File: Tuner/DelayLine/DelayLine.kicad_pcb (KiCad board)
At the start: 2 copper layers, 100 x 100 mm, 84 parts, among them J1 Conn_Coaxial, J10 Conn_Coaxial, J11 Conn_Coaxial, J12 Conn_Coaxial, J13 Conn_01x01, J14 Conn_01x01, J15 Conn_01x01, J16 Conn_01x01, J17 Conn_02x10_Odd_Even, J18 Conn_Coaxial, J19 Conn_Coaxial, J2 Conn_Coaxial, J20 Conn_Coaxial, J21 Conn_Coaxial, J22 Conn_Coaxial, J23 Conn_Coaxial, J24 Conn_Coaxial, J25 Conn_01x01, J26 Conn_01x01, J27 Conn_01x01, J28 Conn_01x01, J29 Conn_Coaxial, J3 Conn_Coaxial, J30 Conn_Coaxial, J31 Conn_Coaxial, J4 Conn_Coaxial, J5 Conn_Coaxial, J6 Conn_Coaxial, J7 Conn_Coaxial, J8 Conn_01x02, J9 Conn_01x02

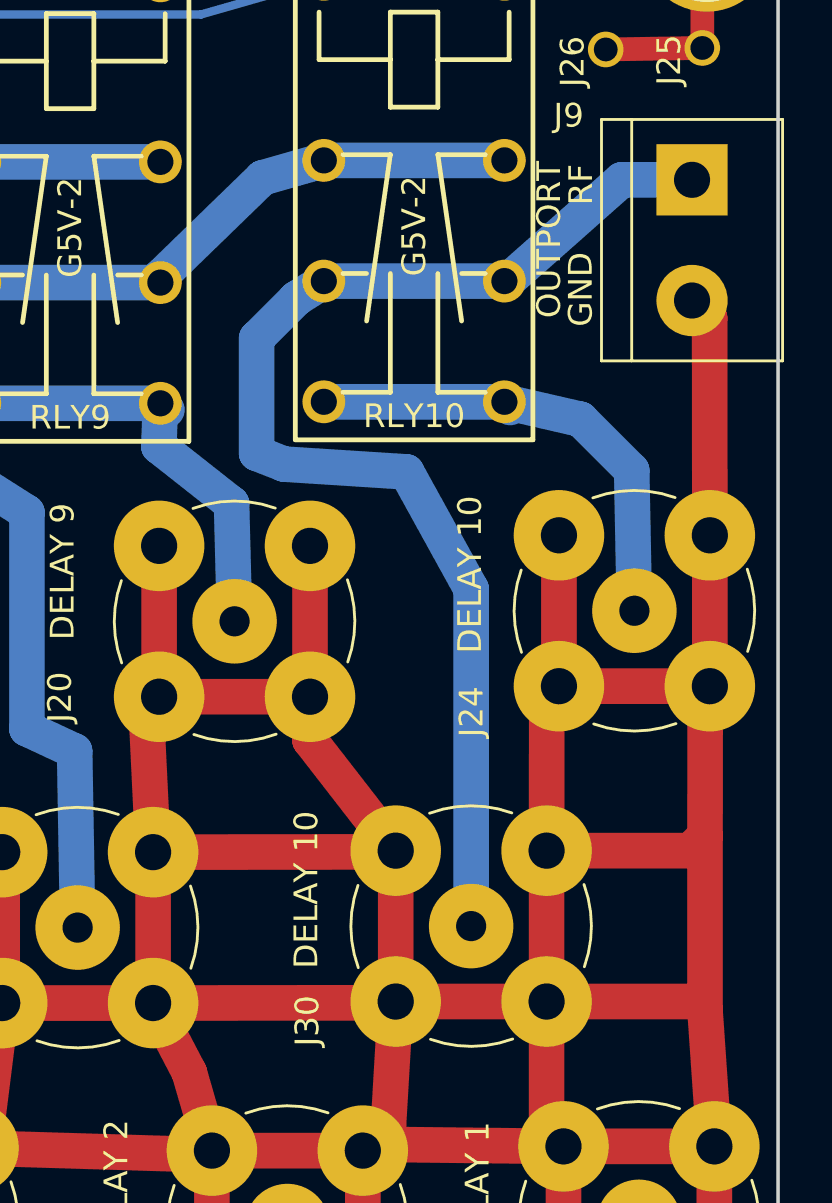
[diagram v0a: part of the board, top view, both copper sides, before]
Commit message: Added phase reversal transformer
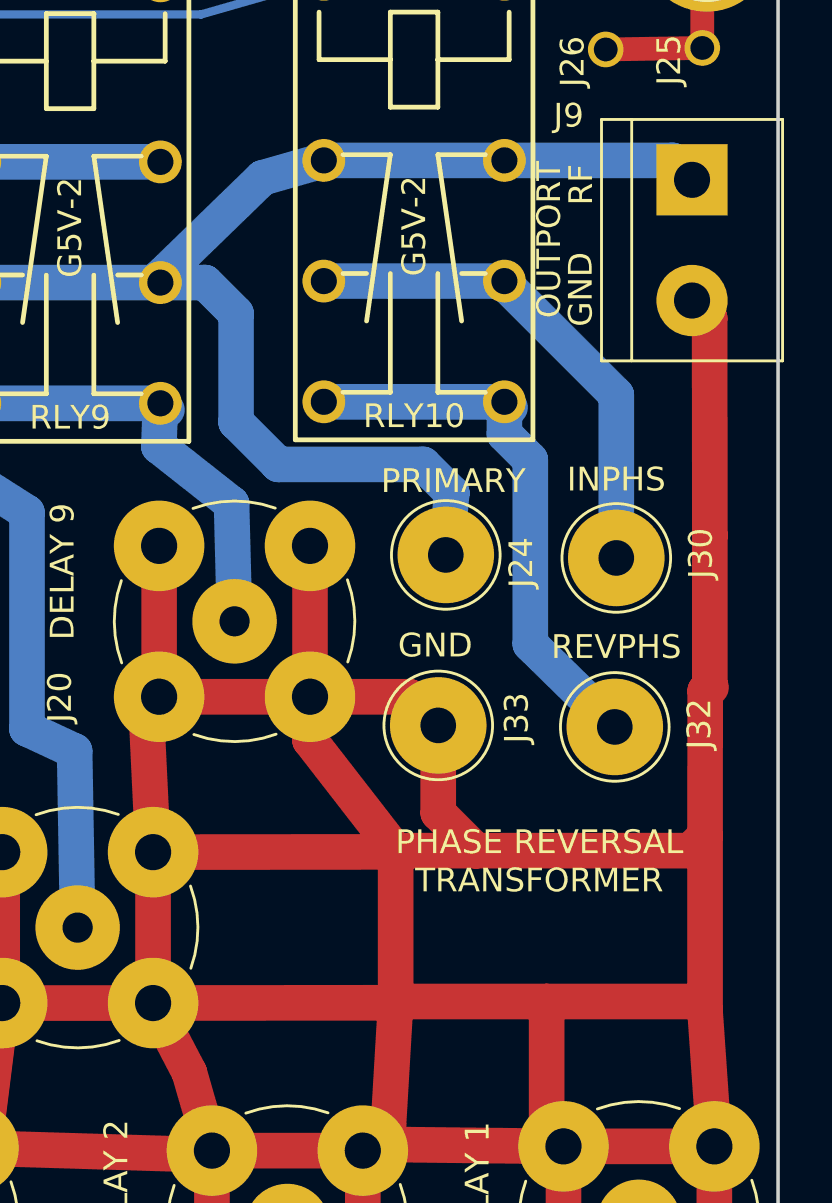
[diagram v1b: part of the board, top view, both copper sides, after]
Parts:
- added J32: Conn_01x01, Connectors:1pin, F.Cu at (143.1, 85.9)
- added J33: Conn_01x01, Connectors:1pin, F.Cu at (135.7, 85.8)
- J24, J30: value Conn_Coaxial -> Conn_01x01; footprint Connectors:bnc-ci -> Connectors:1pin
- moved J30 16.7 mm to (143.2, 78.7)
- moved J24 8.28 mm to (136.0, 78.6)
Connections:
- J24 pad 1: Net-(J24-Pad1) -> Net-(J22-Pad1)
- J9 pad 1: Net-(J30-Pad1) -> Net-(J9-Pad1)
- RLY10 pad 2: Net-(J22-Pad1) -> Net-(J9-Pad1)
- RLY10 pad 4: Net-(J24-Pad1) -> Net-(J32-Pad1)
- RLY10 pad 6: Net-(J22-Pad1) -> Net-(J9-Pad1)
- RLY10 pad 8: Net-(J24-Pad1) -> Net-(J32-Pad1)
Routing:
- net Net-(J30-Pad1): track 51.9 -> 21.3 mm
- net Net-(J32-Pad1): track 0.00 -> 23.6 mm
- net Net-(J24-Pad1): track 20.2 -> 0.00 mm
- net Net-(J9-Pad1): track 0.00 -> 18.5 mm
- net Net-(J22-Pad1): track 57.0 -> 68.0 mm
- net RFGND: track 774.2 -> 765.9 mm
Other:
- board text added: "INPHS"
- board text added: "PHASE REVERSAL TRANSFORMER"
- board text added: "PRIMARY"
- board text added: "REVPHS"
- board text removed: "DELAY 10"

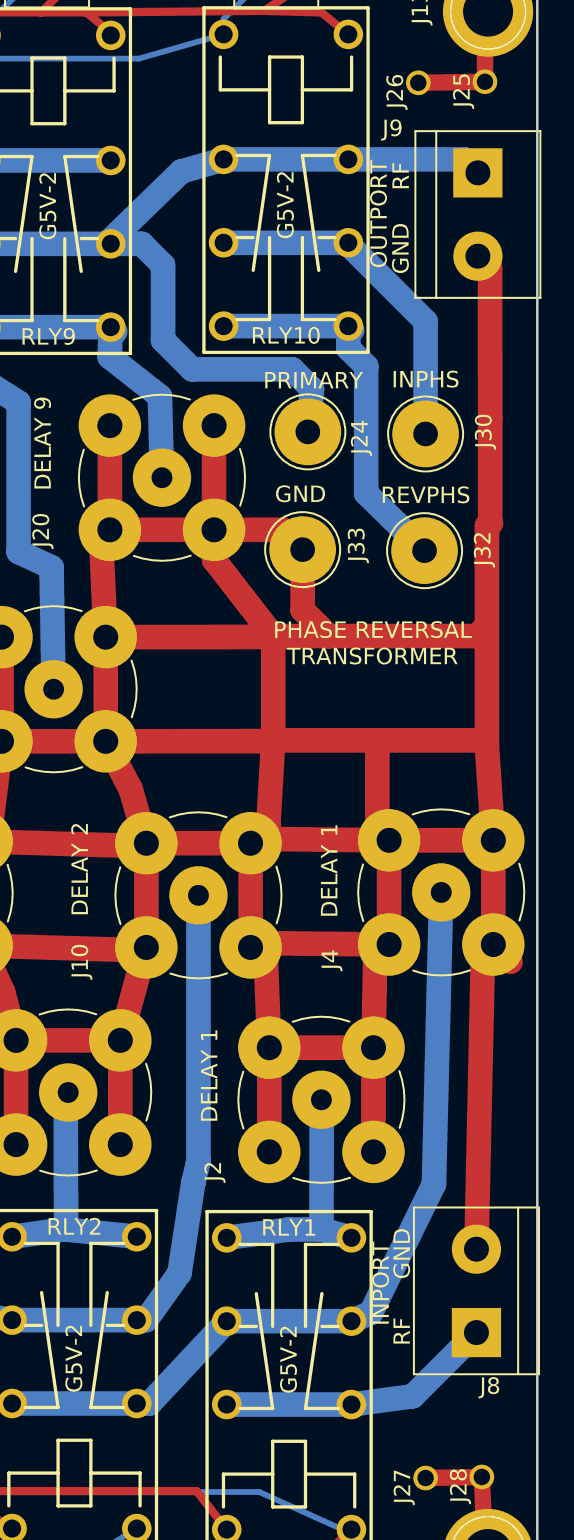
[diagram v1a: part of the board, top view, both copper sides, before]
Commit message: Added Quad Coupler
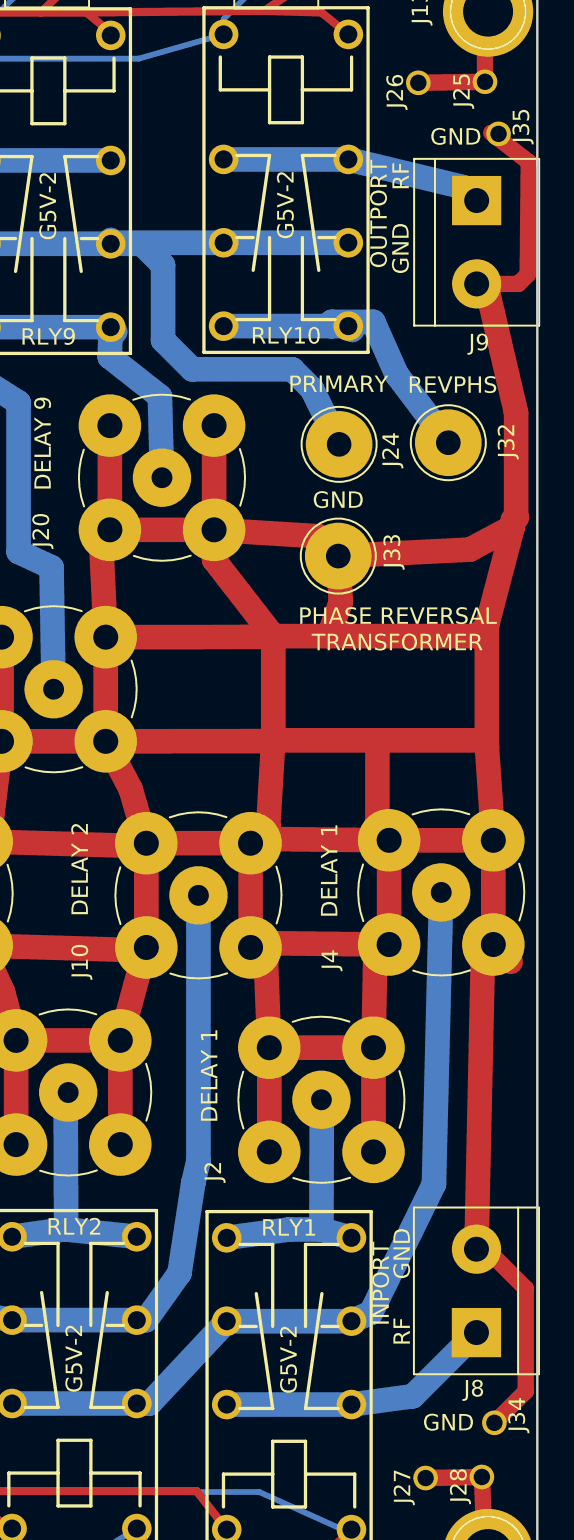
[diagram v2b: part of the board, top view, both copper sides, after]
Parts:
- removed J30: Conn_01x01, Connectors:1pin
- added J34: Conn_01x01, tuner:SOLDERJUMPER, F.Cu at (148.7, 139.0)
- added J35: Conn_01x01, tuner:SOLDERJUMPER, F.Cu at (148.9, 60.5)
- moved J32 6.74 mm to (144.6, 79.3)
- moved J33 2.21 mm to (137.9, 86.2)
- moved J24 2.05 mm to (137.9, 79.4)
- moved J9 1.69 mm to (146.3, 64.5)
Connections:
- RLY10 pad 3: Net-(J30-Pad1) -> Net-(J22-Pad1)
- RLY10 pad 7: Net-(J30-Pad1) -> Net-(J22-Pad1)
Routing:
- net RFGND: track 765.9 -> 802.9 mm
- net Net-(J30-Pad1): track 21.3 -> 0.00 mm
- net Net-(J22-Pad1): track 68.0 -> 77.8 mm
- net Net-(J32-Pad1): track 23.6 -> 19.5 mm
- net Net-(J9-Pad1): track 18.5 -> 16.0 mm
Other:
- board text removed: "INPHS"

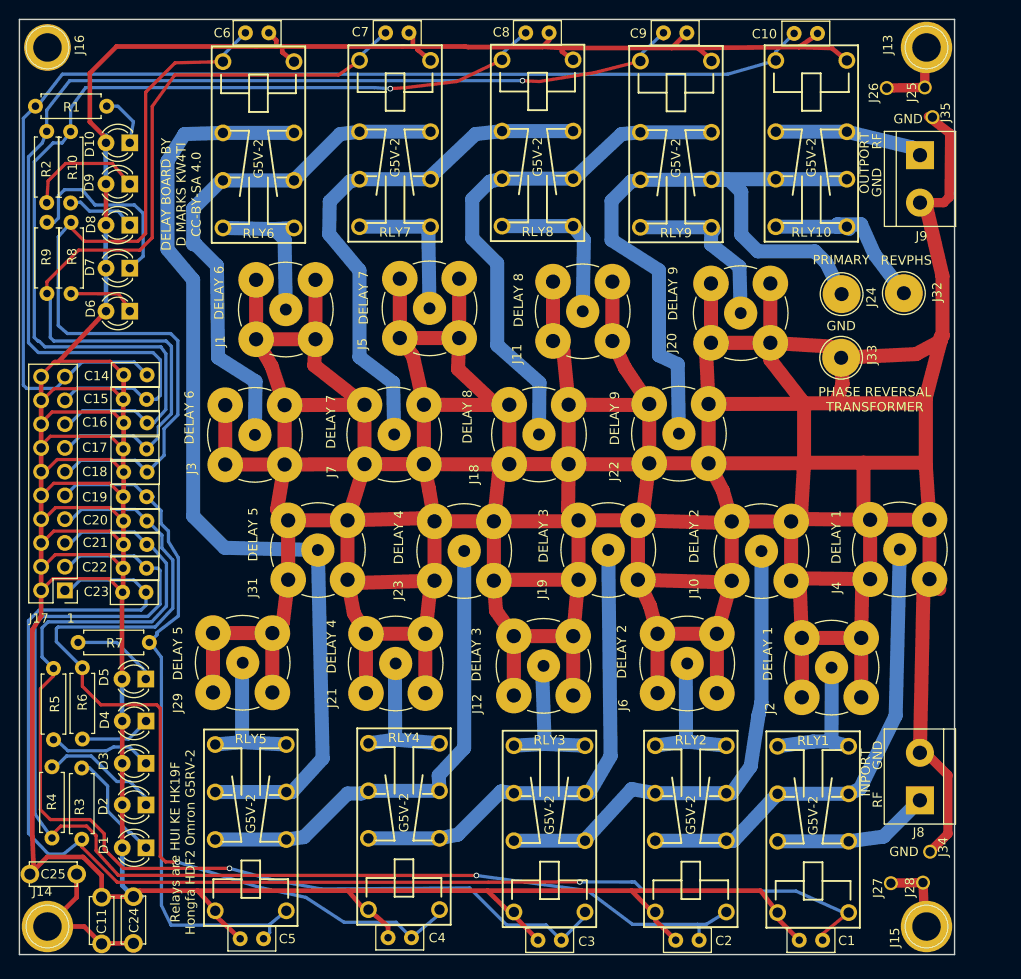
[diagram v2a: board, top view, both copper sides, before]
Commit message: Modified DelayLine to include bypass control
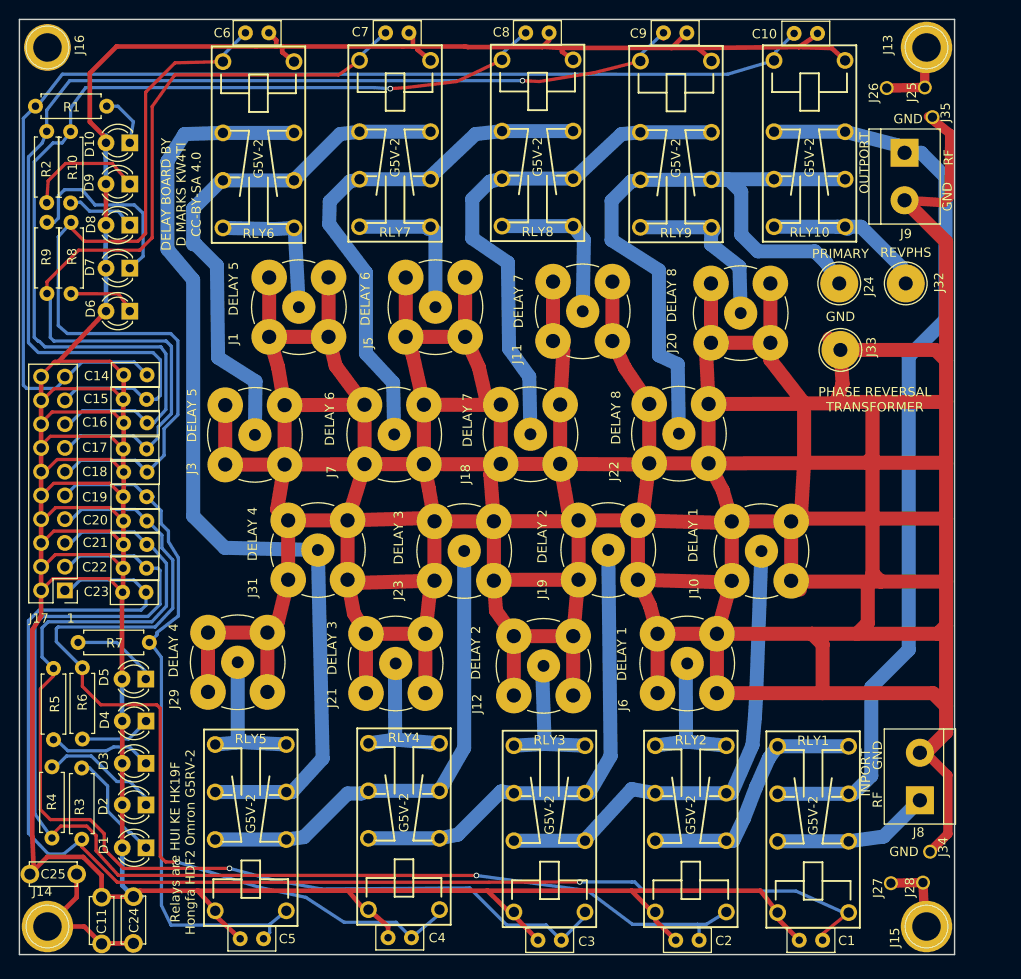
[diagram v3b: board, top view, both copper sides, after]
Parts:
- removed J2, J4: Conn_Coaxial, Connectors:bnc-ci
- moved J9 1.67 mm to (144.7, 64.3)
- moved J1 1.42 mm to (79.9, 80.8)
- moved J24 1.17 mm to (137.7, 78.2)
- moved J32 1.06 mm to (144.8, 78.2)
- moved J18 0.91 mm to (104.6, 94.4)
- moved J33 0.84 mm to (137.8, 85.3)
- moved J5 0.65 mm to (94.5, 80.8)
- moved J29 0.54 mm to (73.3, 118.7)
- moved RLY10 0.19 mm to (134.5, 56.8)
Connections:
- J9 pad 1: Net-(J9-Pad1) -> RFOUT
- RLY1 pad 3: Net-(J4-Pad1) -> RFOUT
- RLY1 pad 4: Net-(J2-Pad1) -> Net-(RLY1-Pad4)
- RLY1 pad 7: Net-(J4-Pad1) -> RFOUT
- RLY1 pad 8: Net-(J2-Pad1) -> Net-(RLY1-Pad4)
- RLY10 pad 2: Net-(J9-Pad1) -> RFOUT
- RLY10 pad 6: Net-(J9-Pad1) -> RFOUT
- RLY2 pad 2: Net-(J4-Pad1) -> Net-(RLY1-Pad4)
- RLY2 pad 6: Net-(J4-Pad1) -> Net-(RLY1-Pad4)
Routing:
- net RFOUT: track 0.00 -> 98.1 mm
- net Net-(J4-Pad1): track 50.7 -> 0.00 mm
- net RFGND: track 802.9 -> 845.1 mm
- net Net-(RLY1-Pad4): track 0.00 -> 27.1 mm
- net Net-(J9-Pad1): track 16.0 -> 0.00 mm
- net Net-(J2-Pad1): track 15.6 -> 0.00 mm
- net Net-(J32-Pad1): track 19.5 -> 17.5 mm
- net Net-(J22-Pad1): track 77.8 -> 76.5 mm
- net Net-(J1-Pad1): track 16.7 -> 16.1 mm
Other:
- board text removed: "DELAY 9"

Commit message: Changed DelayLine to short out sections
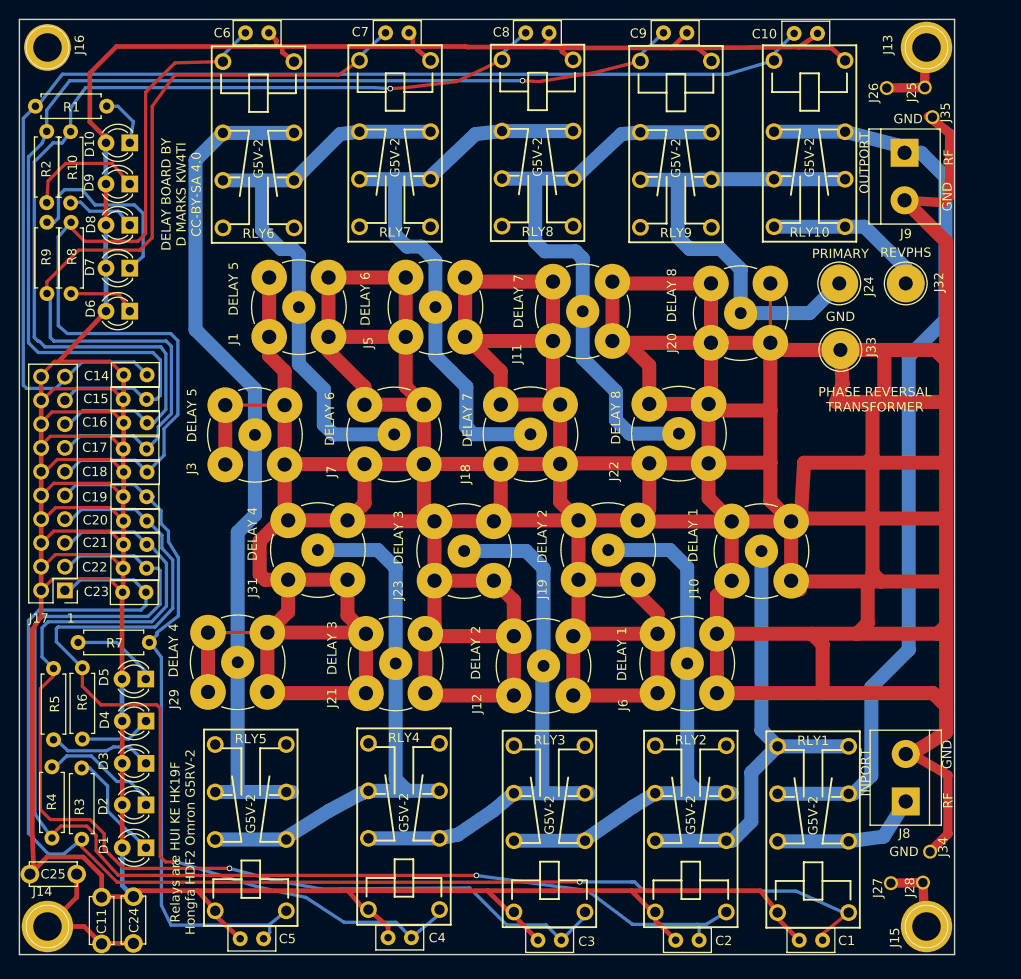
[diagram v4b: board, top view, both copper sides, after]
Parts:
- moved J8 1.52 mm to (144.8, 133.6)
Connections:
- J22 pad 1: Net-(J22-Pad1) -> Net-(J11-Pad1)
- J23 pad 1: Net-(J23-Pad1) -> Net-(J12-Pad1)
- J24 pad 1: Net-(J22-Pad1) -> Net-(J20-Pad1)
- J3 pad 1: Net-(J3-Pad1) -> Net-(J29-Pad1)
- J31 pad 1: Net-(J31-Pad1) -> Net-(J21-Pad1)
- J5 pad 1: Net-(J5-Pad1) -> Net-(J18-Pad1)
- J6 pad 1: Net-(J6-Pad1) -> Net-(J19-Pad1)
- J7 pad 1: Net-(J7-Pad1) -> Net-(J1-Pad1)
- RLY1 pad 4: Net-(RLY1-Pad4) -> Net-(J10-Pad1)
- RLY1 pad 8: Net-(RLY1-Pad4) -> Net-(J10-Pad1)
- RLY10 pad 3: Net-(J22-Pad1) -> Net-(J20-Pad1)
- RLY10 pad 7: Net-(J22-Pad1) -> Net-(J20-Pad1)
- RLY2 pad 2: Net-(RLY1-Pad4) -> Net-(J10-Pad1)
- RLY2 pad 3: Net-(J10-Pad1) -> Net-(J19-Pad1)
- RLY2 pad 4: Net-(J6-Pad1) -> (no net)
- RLY2 pad 6: Net-(RLY1-Pad4) -> Net-(J10-Pad1)
- RLY2 pad 7: Net-(J10-Pad1) -> Net-(J19-Pad1)
- RLY2 pad 8: Net-(J6-Pad1) -> (no net)
- RLY3 pad 2: Net-(J10-Pad1) -> Net-(J19-Pad1)
- RLY3 pad 3: Net-(J19-Pad1) -> Net-(J12-Pad1)
- RLY3 pad 4: Net-(J12-Pad1) -> (no net)
- RLY3 pad 6: Net-(J10-Pad1) -> Net-(J19-Pad1)
- RLY3 pad 7: Net-(J19-Pad1) -> Net-(J12-Pad1)
- RLY3 pad 8: Net-(J12-Pad1) -> (no net)
- RLY4 pad 2: Net-(J19-Pad1) -> Net-(J12-Pad1)
- RLY4 pad 3: Net-(J23-Pad1) -> Net-(J21-Pad1)
- RLY4 pad 4: Net-(J21-Pad1) -> (no net)
- RLY4 pad 6: Net-(J19-Pad1) -> Net-(J12-Pad1)
- RLY4 pad 7: Net-(J23-Pad1) -> Net-(J21-Pad1)
- RLY4 pad 8: Net-(J21-Pad1) -> (no net)
- RLY5 pad 2: Net-(J23-Pad1) -> Net-(J21-Pad1)
- RLY5 pad 3: Net-(J31-Pad1) -> Net-(J29-Pad1)
- RLY5 pad 4: Net-(J29-Pad1) -> (no net)
- RLY5 pad 6: Net-(J23-Pad1) -> Net-(J21-Pad1)
- RLY5 pad 7: Net-(J31-Pad1) -> Net-(J29-Pad1)
- RLY5 pad 8: Net-(J29-Pad1) -> (no net)
- RLY6 pad 2: Net-(J31-Pad1) -> Net-(J29-Pad1)
- RLY6 pad 3: Net-(J3-Pad1) -> Net-(J1-Pad1)
- RLY6 pad 4: Net-(J1-Pad1) -> (no net)
- RLY6 pad 6: Net-(J31-Pad1) -> Net-(J29-Pad1)
- RLY6 pad 7: Net-(J3-Pad1) -> Net-(J1-Pad1)
- RLY6 pad 8: Net-(J1-Pad1) -> (no net)
- RLY7 pad 2: Net-(J3-Pad1) -> Net-(J1-Pad1)
- RLY7 pad 3: Net-(J7-Pad1) -> Net-(J18-Pad1)
- RLY7 pad 4: Net-(J5-Pad1) -> (no net)
- RLY7 pad 6: Net-(J3-Pad1) -> Net-(J1-Pad1)
- RLY7 pad 7: Net-(J7-Pad1) -> Net-(J18-Pad1)
- RLY7 pad 8: Net-(J5-Pad1) -> (no net)
- RLY8 pad 2: Net-(J7-Pad1) -> Net-(J18-Pad1)
- RLY8 pad 3: Net-(J18-Pad1) -> Net-(J11-Pad1)
- RLY8 pad 4: Net-(J11-Pad1) -> (no net)
- RLY8 pad 6: Net-(J7-Pad1) -> Net-(J18-Pad1)
- RLY8 pad 7: Net-(J18-Pad1) -> Net-(J11-Pad1)
- RLY8 pad 8: Net-(J11-Pad1) -> (no net)
- RLY9 pad 2: Net-(J18-Pad1) -> Net-(J11-Pad1)
- RLY9 pad 3: Net-(J22-Pad1) -> Net-(J20-Pad1)
- RLY9 pad 4: Net-(J20-Pad1) -> (no net)
- RLY9 pad 6: Net-(J18-Pad1) -> Net-(J11-Pad1)
- RLY9 pad 7: Net-(J22-Pad1) -> Net-(J20-Pad1)
- RLY9 pad 8: Net-(J20-Pad1) -> (no net)
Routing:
- net Net-(J31-Pad1): track 104.2 -> 0.00 mm
- net Net-(J22-Pad1): track 76.5 -> 0.00 mm
- net Net-(J29-Pad1): track 16.7 -> 91.4 mm
- net RFGND: track 845.1 -> 906.3 mm
- net Net-(J7-Pad1): track 56.4 -> 0.00 mm
- net Net-(J3-Pad1): track 56.3 -> 0.00 mm
- net Net-(J23-Pad1): track 52.3 -> 0.00 mm
- net Net-(J1-Pad1): track 16.1 -> 62.0 mm
- net Net-(J11-Pad1): track 17.6 -> 62.9 mm
- net Net-(J21-Pad1): track 16.0 -> 60.1 mm
- net Net-(J12-Pad1): track 16.0 -> 58.6 mm
- net Net-(J20-Pad1): track 18.7 -> 53.3 mm
- net Net-(RLY1-Pad4): track 27.1 -> 0.00 mm
- net Net-(J5-Pad1): track 16.8 -> 0.00 mm
- net Net-(J6-Pad1): track 16.1 -> 0.00 mm
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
